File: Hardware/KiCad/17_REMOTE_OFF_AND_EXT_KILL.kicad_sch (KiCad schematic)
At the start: 0 parts

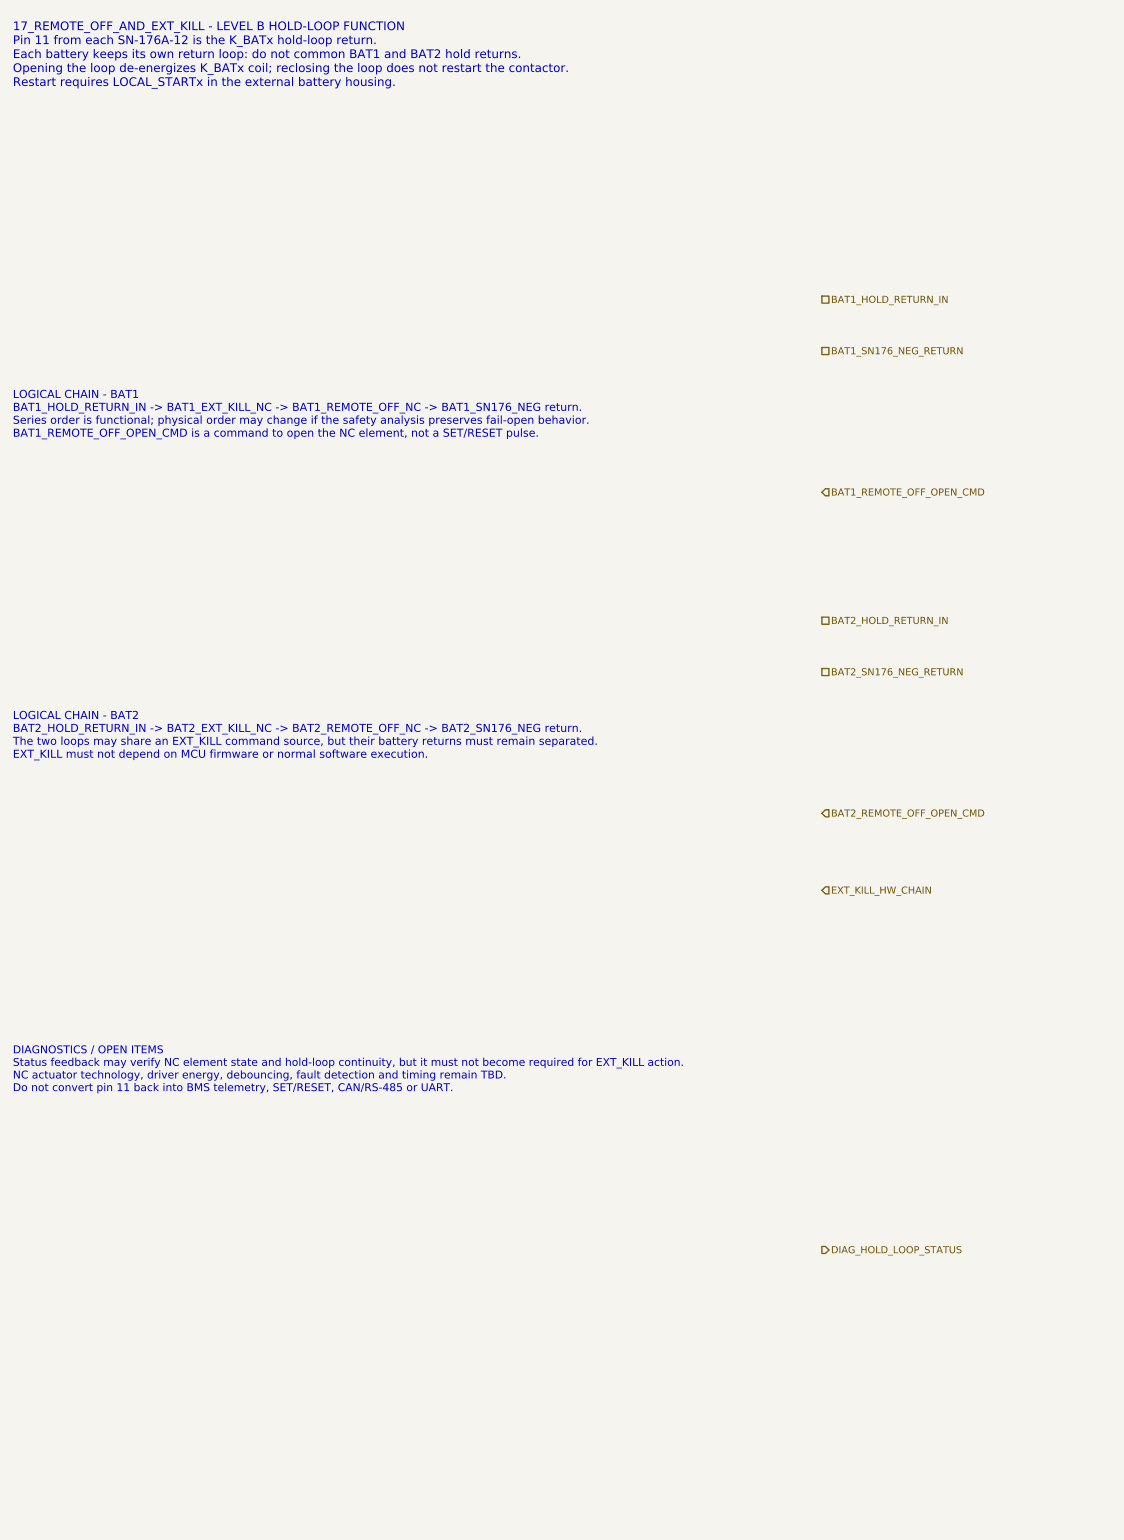
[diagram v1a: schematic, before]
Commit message: hardware: add hold-loop actuator skeleton zones
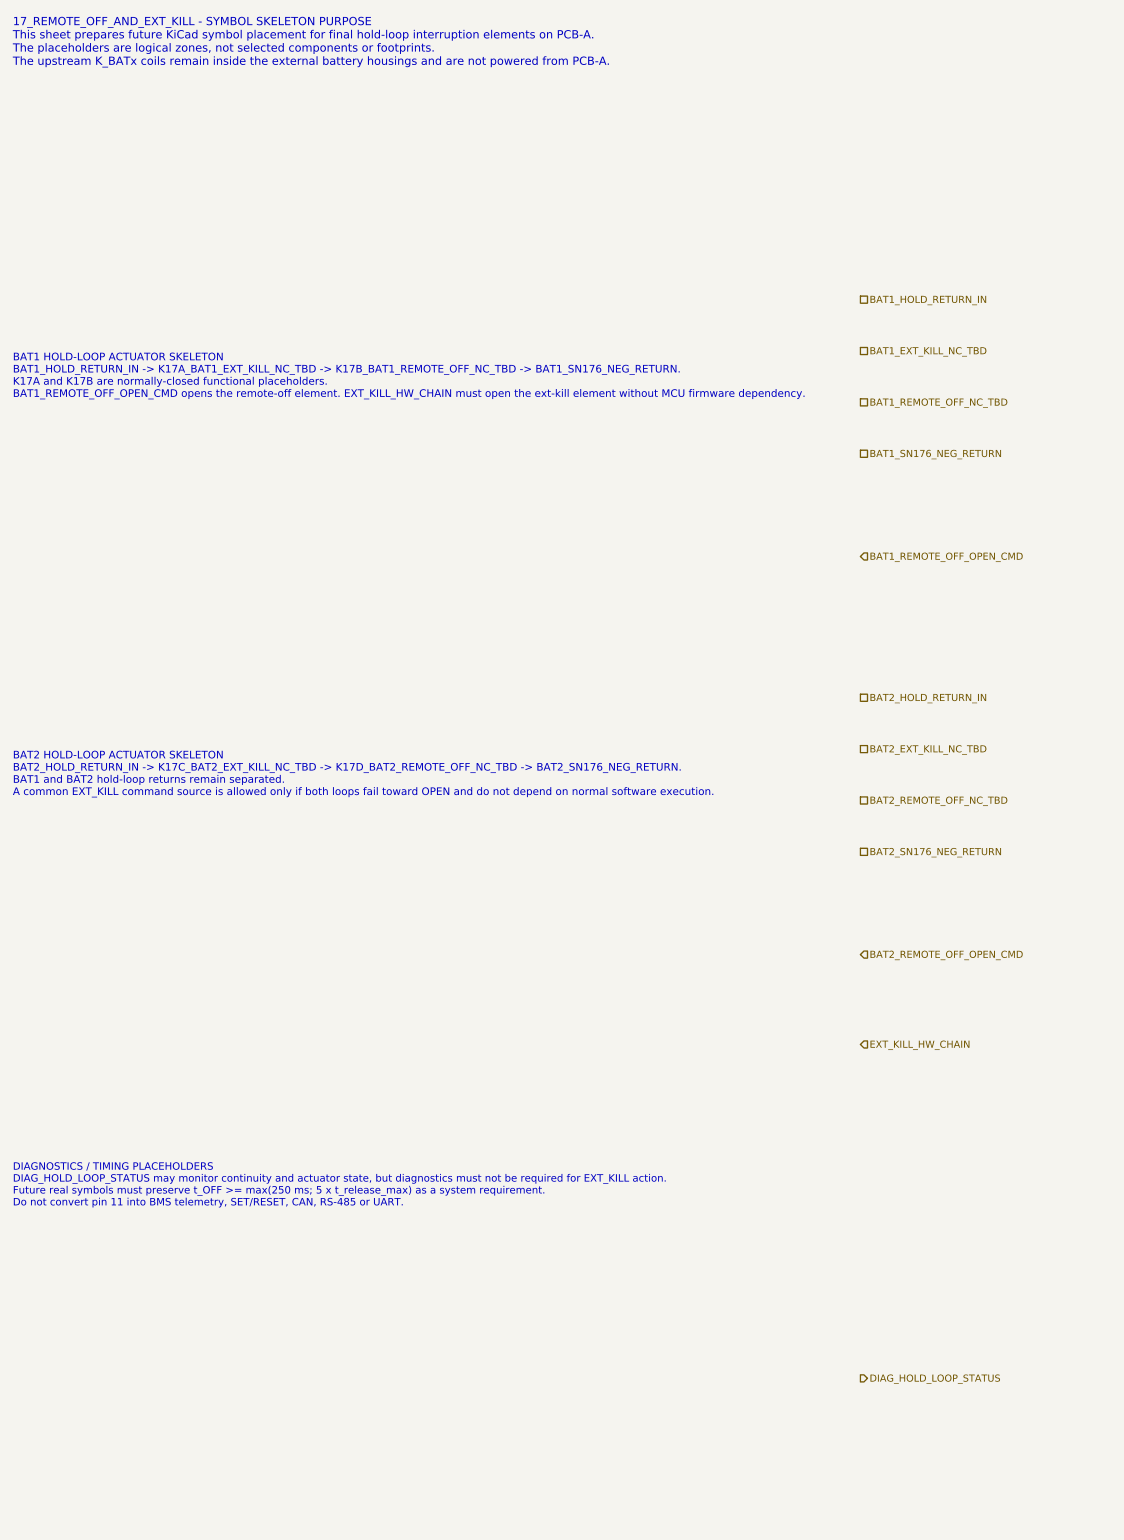
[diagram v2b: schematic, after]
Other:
- note added: "17_REMOTE_OFF_AND_EXT_KILL - SYMBOL SKELETON PURPOSE This sheet prepares future KiCad symbol placement for final hold-loop interruption elements on PCB-A. The placeholders are logical zones, not selected components or footprints. The upstream K_BATx coils remain inside the external battery housings and are not powered from PCB-A."
- note added: "BAT1 HOLD-LOOP ACTUATOR SKELETON BAT1_HOLD_RETURN_IN -> K17A_BAT1_EXT_KILL_NC_TBD -> K17B_BAT1_REMOTE_OFF_NC_TBD -> BAT1_SN176_NEG_RETURN. K17A and K17B are normally-closed functional placeholders. BAT1_REMOTE_OFF_OPEN_CMD opens the remote-off element. EXT_KILL_HW_CHAIN must open the ext-kill element without MCU firmware dependency."
- note added: "BAT2 HOLD-LOOP ACTUATOR SKELETON BAT2_HOLD_RETURN_IN -> K17C_BAT2_EXT_KILL_NC_TBD -> K17D_BAT2_REMOTE_OFF_NC_TBD -> BAT2_SN176_NEG_RETURN. BAT1 and BAT2 hold-loop returns remain separated. A common EXT_KILL command source is allowed only if both loops fail toward OPEN and do not depend on normal software execution."
- note added: "DIAGNOSTICS / TIMING PLACEHOLDERS DIAG_HOLD_LOOP_STATUS may monitor continuity and actuator state, but diagnostics must not be required for EXT_KILL action. Future real symbols must preserve t_OFF >= max(250 ms; 5 x t_release_max) as a system requirement. Do not convert pin 11 into BMS telemetry, SET/RESET, CAN, RS-485 or UART."
- note removed: "17_REMOTE_OFF_AND_EXT_KILL - LEVEL B HOLD-LOOP FUNCTION Pin 11 from each SN-176A-12 is the K_BATx hold-loop return. Each battery keeps its own return loop: do not common BAT1 and BAT2 hold returns. Opening the loop de-energizes K_BATx coil; reclosing the loop does not restart the contactor. Restart requires LOCAL_STARTx in the external battery housing."
- note removed: "DIAGNOSTICS / OPEN ITEMS Status feedback may verify NC element state and hold-loop continuity, but it must not become required for EXT_KILL action. NC actuator technology, driver energy, debouncing, fault detection and timing remain TBD. Do not convert pin 11 back into BMS telemetry, SET/RESET, CAN/RS-485 or UART."
- note removed: "LOGICAL CHAIN - BAT1 BAT1_HOLD_RETURN_IN -> BAT1_EXT_KILL_NC -> BAT1_REMOTE_OFF_NC -> BAT1_SN176_NEG return. Series order is functional; physical order may change if the safety analysis preserves fail-open behavior. BAT1_REMOTE_OFF_OPEN_CMD is a command to open the NC element, not a SET/RESET pulse."
- note removed: "LOGICAL CHAIN - BAT2 BAT2_HOLD_RETURN_IN -> BAT2_EXT_KILL_NC -> BAT2_REMOTE_OFF_NC -> BAT2_SN176_NEG return. The two loops may share an EXT_KILL command source, but their battery returns must remain separated. EXT_KILL must not depend on MCU firmware or normal software execution."
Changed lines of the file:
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@@
 		(title "17_REMOTE_OFF_AND_EXT_KILL - hold-loop final actuators")
 		(date "2026-07-15")
-		(rev "B1")
+		(rev "C0")
 		(company "Gonoboben/plataVM")
-		(comment 1 "Architecture Level B: hold-loop return interruption and safe-state rules")
-		(comment 2 "No relay/MOSFET/contact implementation selected")
+		(comment 1 "Symbol skeleton: NC actuator placement zones for K_BATx hold-loop interruption")
+		(comment 2 "Text-only placeholders; no relay, MOSFET, optocoupler or driver topology selected")
 	)
-	(text "17_REMOTE_OFF_AND_EXT_KILL - LEVEL B HOLD-LOOP FUNCTION\nPin 11 from each SN-176A-12 is the K_BATx hold-loop return.\nEach battery keeps its own return loop: do not common BAT1 and BAT2 hold returns.\nOpening the loop de-energizes K_BATx coil; reclosing the loop does not restart the contactor.\nRestart requires LOCAL_STARTx in the external battery housing."
+	(text "17_REMOTE_OFF_AND_EXT_KILL - SYMBOL SKELETON PURPOSE\nThis sheet prepares future KiCad symbol placement for final hold-loop interruption elements on PCB-A.\nThe placeholders are logical zones, not selected components or footprints.\nThe upstream K_BATx coils remain inside the external battery housings and are not powered from PCB-A."
 		(exclude_from_sim no)
-		(at 12 16 0)
-		(effects (font (size 1.35 1.35)) (justify left))
-		(uuid "bfe-dh-00000017-0000-4000-8000-000000000101")
+		(at 12 14 0)
+		(effects (font (size 1.28 1.28)) (justify left))
+		(uuid "bfe-symbol-00000017-0000-4000-8000-000000000101")
 	)
-	(text "LOGICAL CHAIN - BAT1\nBAT1_HOLD_RETURN_IN -> BAT1_EXT_KILL_NC -> BAT1_REMOTE_OFF_NC -> BAT1_SN176_NEG return.\nSeries order is functional; physical order may change if the safety analysis preserves fail-open behavior.\nBAT1_REMOTE_OFF_OPEN_CMD is a command to open the NC element, not a SET/RESET pulse."
+	(text "BAT1 HOLD-LOOP ACTUATOR SKELETON\nBAT1_HOLD_RETURN_IN -> K17A_BAT1_EXT_KILL_NC_TBD -> K17B_BAT1_REMOTE_OFF_NC_TBD -> BAT1_SN176_NEG_RETURN.\nK17A and K17B are normally-closed functional placeholders.\nBAT1_REMOTE_OFF_OPEN_CMD opens the remote-off element. EXT_KILL_HW_CHAIN must open the ext-kill element without MCU firmware dependency."
 		(exclude_from_sim no)
-		(at 12 72 0)
-		(effects (font (size 1.25 1.25)) (justify left))
-		(uuid "bfe-dh-00000017-0000-4000-8000-000000000102")
+		(at 12 66 0)
+		(effects (font (size 1.18 1.18)) (justify left))
+		(uuid "bfe-symbol-00000017-0000-4000-8000-000000000102")
 	)
-	(text "LOGICAL CHAIN - BAT2\nBAT2_HOLD_RETURN_IN -> BAT2_EXT_KILL_NC -> BAT2_REMOTE_OFF_NC -> BAT2_SN176_NEG return.\nThe two loops may share an EXT_KILL command source, but their battery returns must remain separated.\nEXT_KILL must not depend on MCU firmware or normal software execution."
+	(text "BAT2 HOLD-LOOP ACTUATOR SKELETON\nBAT2_HOLD_RETURN_IN -> K17C_BAT2_EXT_KILL_NC_TBD -> K17D_BAT2_REMOTE_OFF_NC_TBD -> BAT2_SN176_NEG_RETURN.\nBAT1 and BAT2 hold-loop returns remain separated.\nA common EXT_KILL command source is allowed only if both loops fail toward OPEN and do not depend on normal software execution."
 		(exclude_from_sim no)
-		(at 12 122 0)
-		(effects (font (size 1.25 1.25)) (justify left))
-		(uuid "bfe-dh-00000017-0000-4000-8000-000000000103")
+		(at 12 128 0)
+		(effects (font (size 1.18 1.18)) (justify left))
+		(uuid "bfe-symbol-00000017-0000-4000-8000-000000000103")
 	)
-	(text "DIAGNOSTICS / OPEN ITEMS\nStatus feedback may verify NC element state and hold-loop continuity, but it must not become required for EXT_KILL action.\nNC actuator technology, driver energy, debouncing, fault detection and timing remain TBD.\nDo not convert pin 11 back into BMS telemetry, SET/RESET, CAN/RS-485 or UART."
+	(text "DIAGNOSTICS / TIMING PLACEHOLDERS\nDIAG_HOLD_LOOP_STATUS may monitor continuity and actuator state, but diagnostics must not be required for EXT_KILL action.\nFuture real symbols must preserve t_OFF >= max(250 ms; 5 x t_release_max) as a system requirement.\nDo not convert pin 11 into BMS telemetry, SET/RESET, CAN, RS-485 or UART."
 		(exclude_from_sim no)
-		(at 12 174 0)
-		(effects (font (size 1.22 1.22)) (justify left))
-		(uuid "bfe-dh-00000017-0000-4000-8000-000000000104")
+		(at 12 192 0)
+		(effects (font (size 1.15 1.15)) (justify left))
+		(uuid "bfe-symbol-00000017-0000-4000-8000-000000000104")
 	)
-	(hierarchical_label "BAT1_HOLD_RETURN_IN" (shape passive) (exclude_from_sim no) (at 138 54 0) (effects (font (size 1.1 1.1)) (justify left)) (uuid "bfe-dh-00000017-0000-4000-8000-000000000201"))
-	(hierarchical_label "BAT1_SN176_NEG_RETURN" (shape passive) (exclude_from_sim no) (at 138 62 0) (effects (font (size 1.1 1.1)) (justify left)) (uuid "bfe-dh-00000017-0000-4000-8000-000000000202"))
-	(hierarchical_label "BAT2_HOLD_RETURN_IN" (shape passive) (exclude_from_sim no) (at 138 104 0) (effects (font (size 1.1 1.1)) (justify left)) (uuid "bfe-dh-00000017-0000-4000-8000-000000000203"))
-	(hierarchical_label "BAT2_SN176_NEG_RETURN" (shape passive) (exclude_from_sim no) (at 138 112 0) (effects (font (size 1.1 1.1)) (justify left)) (uuid "bfe-dh-00000017-0000-4000-8000-000000000204"))
-	(hierarchical_label "BAT1_REMOTE_OFF_OPEN_CMD" (shape input) (exclude_from_sim no) (at 138 84 0) (effects (font (size 1.1 1.1)) (justify left)) (uuid "bfe-dh-00000017-0000-4000-8000-000000000205"))
-	(hierarchical_label "BAT2_REMOTE_OFF_OPEN_CMD" (shape input) (exclude_from_sim no) (at 138 134 0) (effects (font (size 1.1 1.1)) (justify left)) (uuid "bfe-dh-00000017-0000-4000-8000-000000000206"))
-	(hierarchical_label "EXT_KILL_HW_CHAIN" (shape input) (exclude_from_sim no) (at 138 146 0) (effects (font (size 1.1 1.1)) (justify left)) (uuid "bfe-dh-00000017-0000-4000-8000-000000000207"))
-	(hierarchical_label "DIAG_HOLD_LOOP_STATUS" (shape output) (exclude_from_sim no) (at 138 202 0) (effects (font (size 1.1 1.1)) (justify left)) (uuid "bfe-dh-00000017-0000-4000-8000-000000000208"))
+	(hierarchical_label "BAT1_HOLD_RETURN_IN" (shape passive) (exclude_from_sim no) (at 144 54 0) (effects (font (size 1.1 1.1)) (justify left)) (uuid "bfe-symbol-00000017-0000-4000-8000-000000000201"))
+	(hierarchical_label "BAT1_EXT_KILL_NC_TBD" (shape passive) (exclude_from_sim no) (at 144 62 0) (effects (font (size 1.1 1.1)) (justify left)) (uuid "bfe-symbol-00000017-0000-4000-8000-000000000202"))
+	(hierarchical_label "BAT1_REMOTE_OFF_NC_TBD" (shape passive) (exclude_from_sim no) (at 144 70 0) (effects (font (size 1.1 1.1)) (justify left)) (uuid "bfe-symbol-00000017-0000-4000-8000-000000000203"))
+	(hierarchical_label "BAT1_SN176_NEG_RETURN" (shape passive) (exclude_from_sim no) (at 144 78 0) (effects (font (size 1.1 1.1)) (justify left)) (uuid "bfe-symbol-00000017-0000-4000-8000-000000000204"))
+	(hierarchical_label "BAT2_HOLD_RETURN_IN" (shape passive) (exclude_from_sim no) (at 144 116 0) (effects (font (size 1.1 1.1)) (justify left)) (uuid "bfe-symbol-00000017-0000-4000-8000-000000000205"))
+	(hierarchical_label "BAT2_EXT_KILL_NC_TBD" (shape passive) (exclude_from_sim no) (at 144 124 0) (effects (font (size 1.1 1.1)) (justify left)) (uuid "bfe-symbol-00000017-0000-4000-8000-000000000206"))
+	(hierarchical_label "BAT2_REMOTE_OFF_NC_TBD" (shape passive) (exclude_from_sim no) (at 144 132 0) (effects (font (size 1.1 1.1)) (justify left)) (uuid "bfe-symbol-00000017-0000-4000-8000-000000000207"))
+	(hierarchical_label "BAT2_SN176_NEG_RETURN" (shape passive) (exclude_from_sim no) (at 144 140 0) (effects (font (size 1.1 1.1)) (justify left)) (uuid "bfe-symbol-00000017-0000-4000-8000-000000000208"))
+	(hierarchical_label "BAT1_REMOTE_OFF_OPEN_CMD" (shape input) (exclude_from_sim no) (at 144 94 0) (effects (font (size 1.1 1.1)) (justify left)) (uuid "bfe-symbol-00000017-0000-4000-8000-000000000209"))
+	(hierarchical_label "BAT2_REMOTE_OFF_OPEN_CMD" (shape input) (exclude_from_sim no) (at 144 156 0) (effects (font (size 1.1 1.1)) (justify left)) (uuid "bfe-symbol-00000017-0000-4000-8000-000000000210"))
+	(hierarchical_label "EXT_KILL_HW_CHAIN" (shape input) (exclude_from_sim no) (at 144 170 0) (effects (font (size 1.1 1.1)) (justify left)) (uuid "bfe-symbol-00000017-0000-4000-8000-000000000211"))
+	(hierarchical_label "DIAG_HOLD_LOOP_STATUS" (shape output) (exclude_from_sim no) (at 144 222 0) (effects (font (size 1.1 1.1)) (justify left)) (uuid "bfe-symbol-00000017-0000-4000-8000-000000000212"))
 )
